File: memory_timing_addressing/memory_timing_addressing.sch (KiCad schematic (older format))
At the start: 1 part, among them P1 DIN_41612_128P

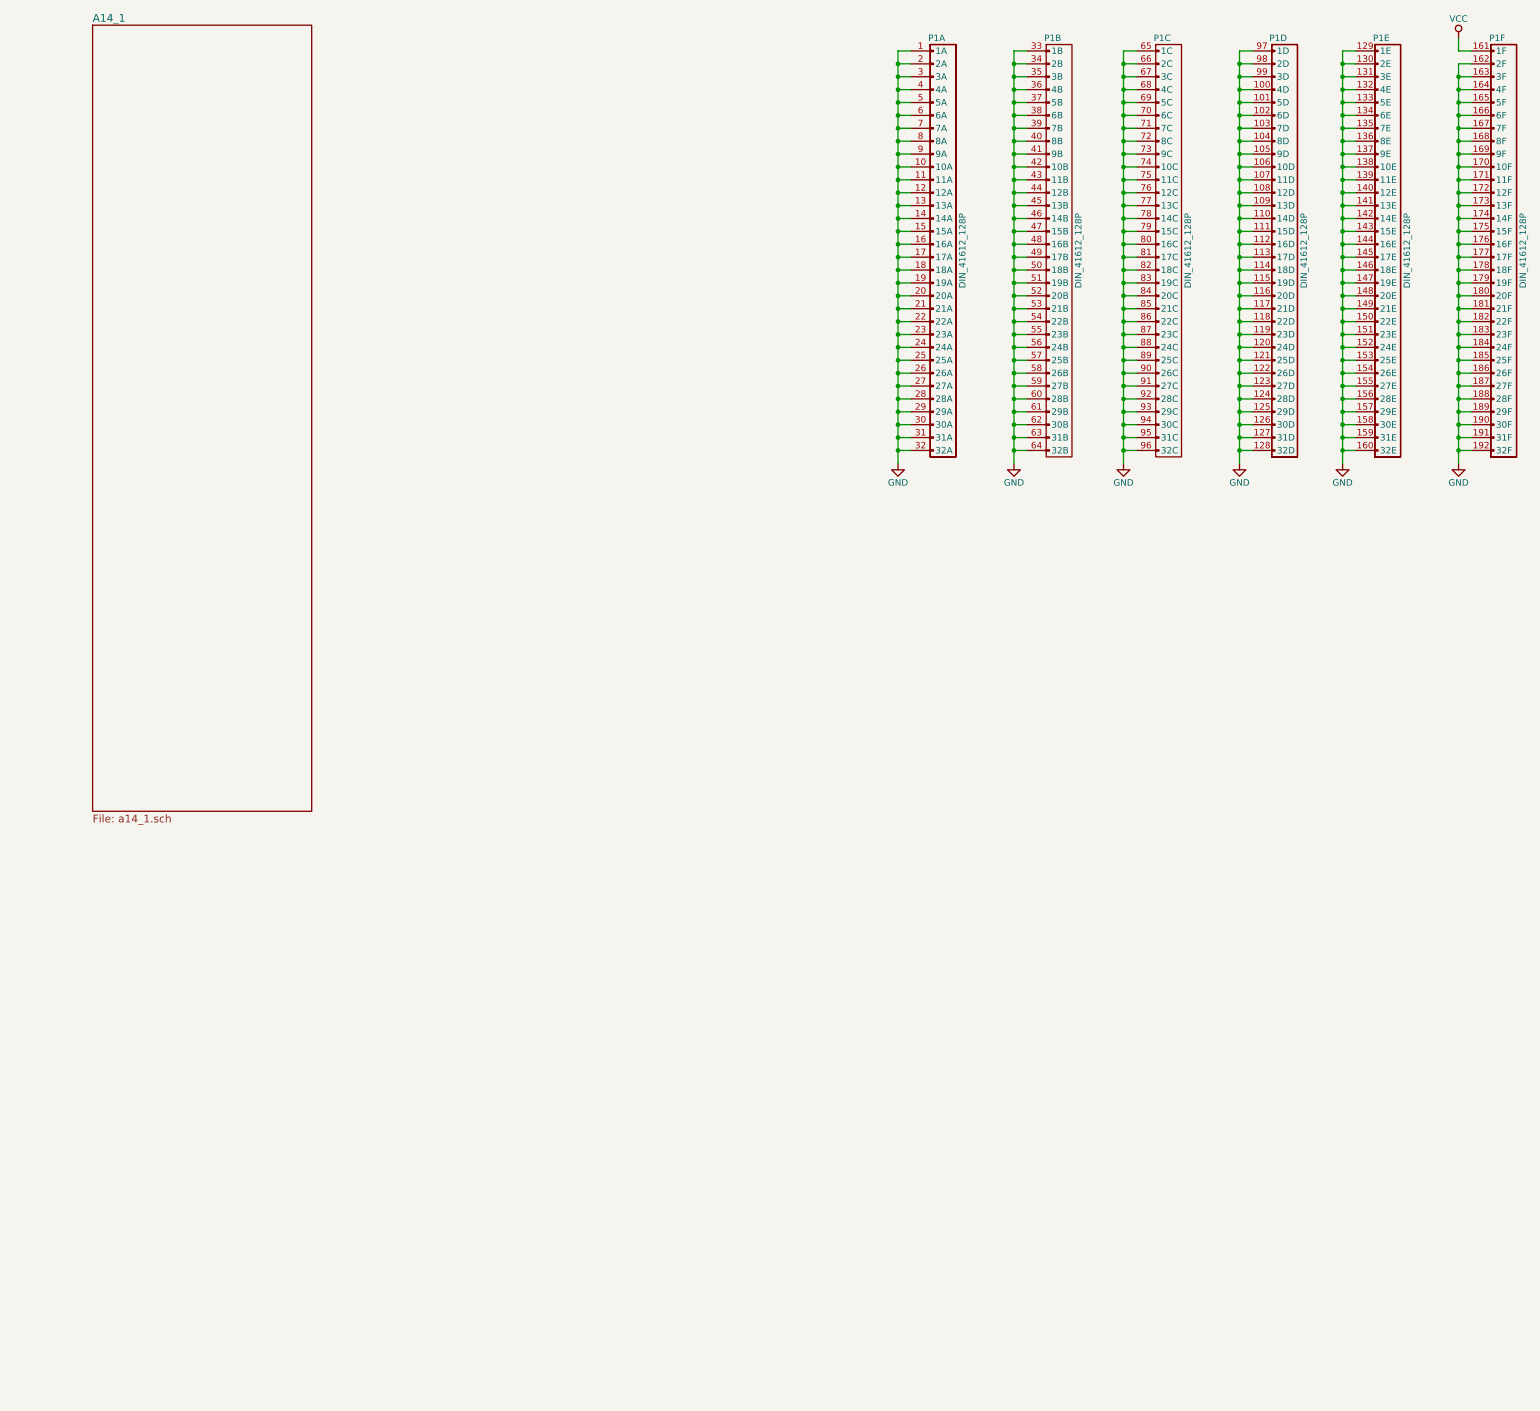
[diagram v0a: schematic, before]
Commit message: Finished off and integrated module 14. Also fixed a couple of bugs this turned up (both initial conditions, and bad wiring in the CGMC pulse generator and S register)
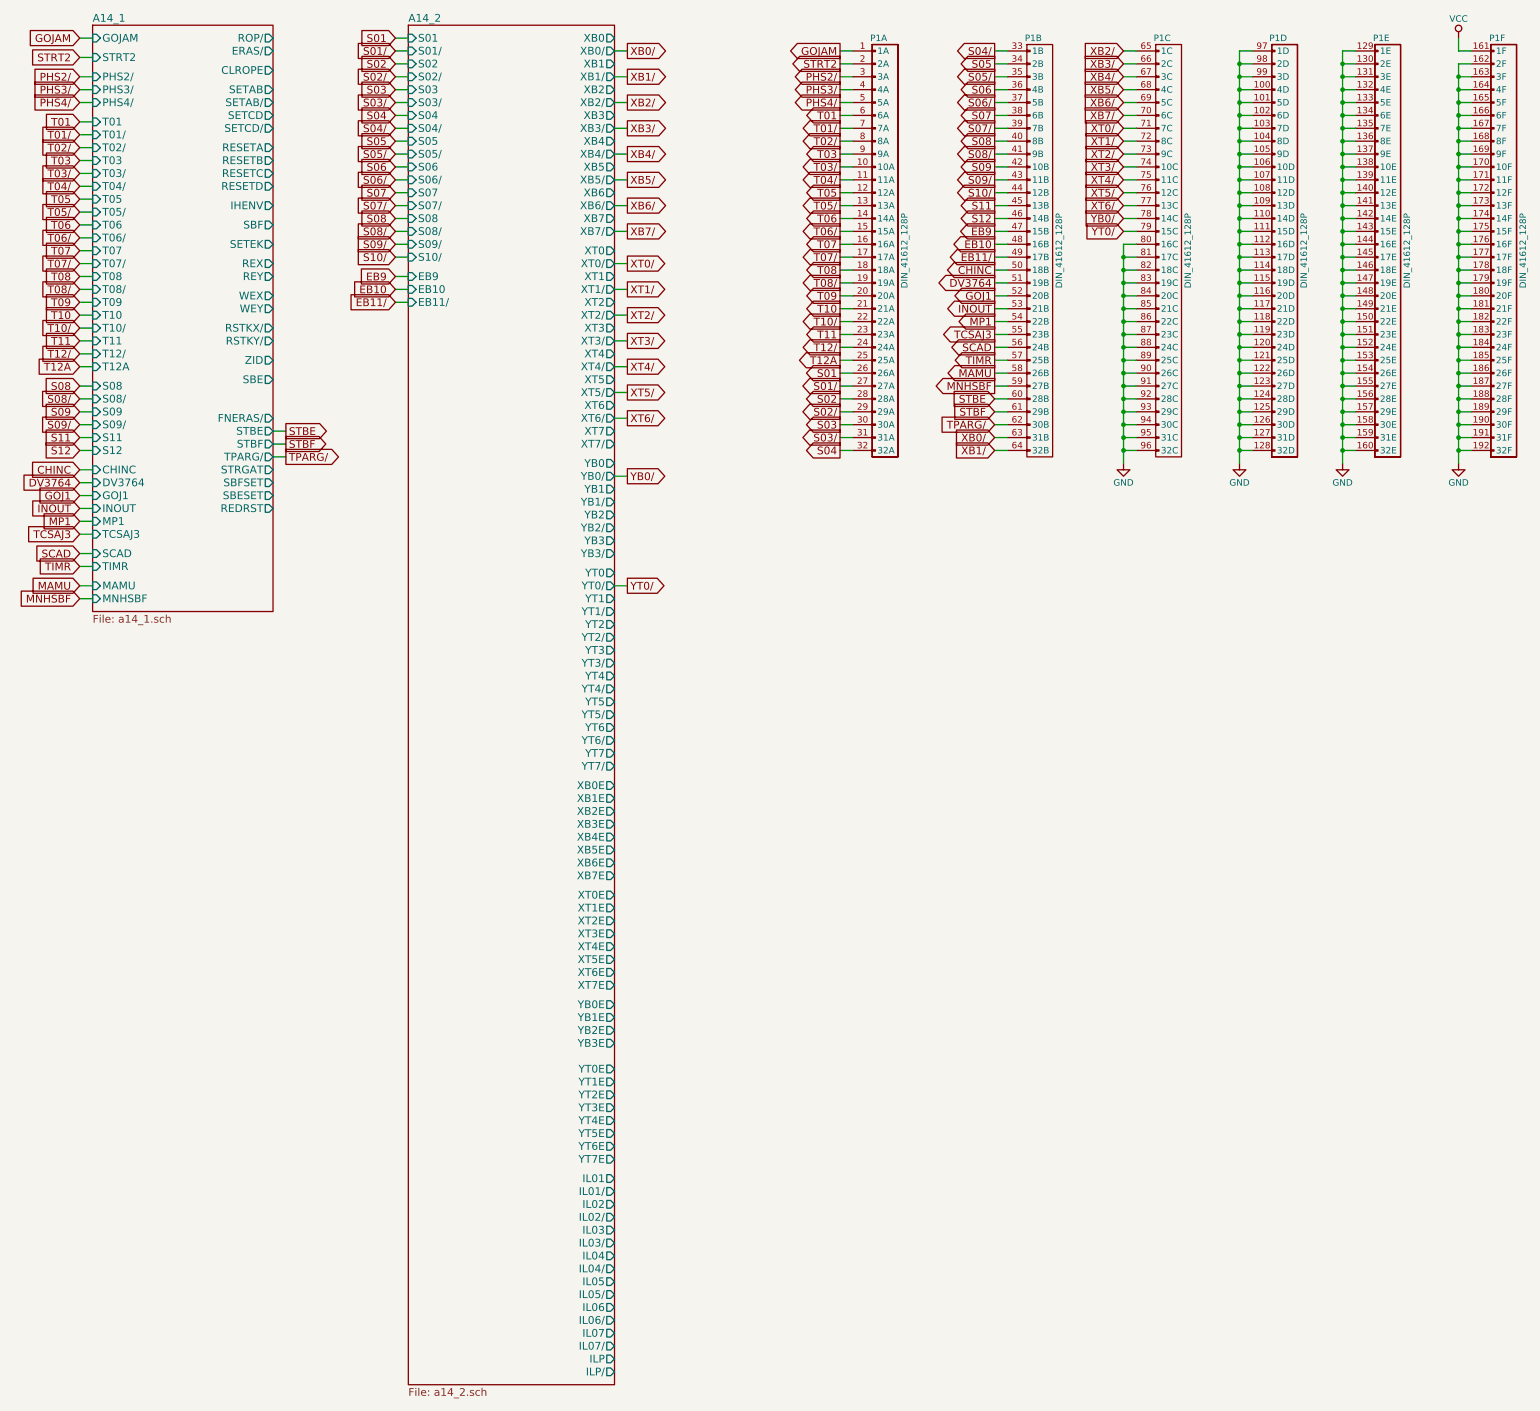
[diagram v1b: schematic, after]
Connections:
- net GND: no longer P1.1 (1A), P1.10 (10A), P1.11 (11A), P1.12 (12A), P1.13 (13A), P1.14 (14A), P1.15 (15A), P1.16 (16A), P1.17 (17A), P1.18 (18A), P1.19 (19A), P1.2 (2A), P1.20 (20A), P1.21 (21A), P1.22 (22A), P1.23 (23A), P1.24 (24A), P1.25 (25A), P1.26 (26A), P1.27 (27A), P1.28 (28A), P1.29 (29A), P1.3 (3A), P1.30 (30A), P1.31 (31A), P1.32 (32A), P1.33 (1B), P1.34 (2B), P1.35 (3B), P1.36 (4B), P1.37 (5B), P1.38 (6B), P1.39 (7B), P1.4 (4A), P1.40 (8B), P1.41 (9B), P1.42 (10B), P1.43 (11B), P1.44 (12B), P1.45 (13B), P1.46 (14B), P1.47 (15B), P1.48 (16B), P1.49 (17B), P1.5 (5A), P1.50 (18B), P1.51 (19B), P1.52 (20B), P1.53 (21B), P1.54 (22B), P1.55 (23B), P1.56 (24B), P1.57 (25B), P1.58 (26B), P1.59 (27B), P1.6 (6A), P1.60 (28B), P1.61 (29B), P1.62 (30B), P1.63 (31B), P1.64 (32B), P1.65 (1C), P1.66 (2C), P1.67 (3C), P1.68 (4C), P1.69 (5C), P1.7 (7A), P1.70 (6C), P1.71 (7C), P1.72 (8C), P1.73 (9C), P1.74 (10C), P1.75 (11C), P1.76 (12C), P1.77 (13C), P1.78 (14C), P1.79 (15C), P1.8 (8A), P1.9 (9A)
- new net CHINC: P1.50 (18B)
- new net DV3764: P1.51 (19B)
- new net EB10: P1.48 (16B)
- new net EB11/: P1.49 (17B)
- new net EB9: P1.47 (15B)
- new net GOJ1: P1.52 (20B)
- new net GOJAM: P1.1 (1A)
- new net INOUT: P1.53 (21B)
- new net MAMU: P1.58 (26B)
- new net MNHSBF: P1.59 (27B)
- new net MP1: P1.54 (22B)
- new net PHS2/: P1.3 (3A)
- new net PHS3/: P1.4 (4A)
- new net PHS4/: P1.5 (5A)
- new net S01: P1.26 (26A)
- new net S01/: P1.27 (27A)
- new net S02: P1.28 (28A)
- new net S02/: P1.29 (29A)
- new net S03: P1.30 (30A)
- new net S03/: P1.31 (31A)
- new net S04: P1.32 (32A)
- new net S04/: P1.33 (1B)
- new net S05: P1.34 (2B)
- new net S05/: P1.35 (3B)
- new net S06: P1.36 (4B)
- new net S06/: P1.37 (5B)
- new net S07: P1.38 (6B)
- new net S07/: P1.39 (7B)
- new net S08: P1.40 (8B)
- new net S08/: P1.41 (9B)
- new net S09: P1.42 (10B)
- new net S09/: P1.43 (11B)
- new net S10/: P1.44 (12B)
- new net S11: P1.45 (13B)
- new net S12: P1.46 (14B)
- new net SCAD: P1.56 (24B)
- new net STBE: P1.60 (28B)
- new net STBF: P1.61 (29B)
- new net STRT2: P1.2 (2A)
- new net T01: P1.6 (6A)
- new net T01/: P1.7 (7A)
- new net T02/: P1.8 (8A)
- new net T03: P1.9 (9A)
- new net T03/: P1.10 (10A)
- new net T04/: P1.11 (11A)
- new net T05: P1.12 (12A)
- new net T05/: P1.13 (13A)
- new net T06: P1.14 (14A)
- new net T06/: P1.15 (15A)
- new net T07: P1.16 (16A)
- new net T07/: P1.17 (17A)
- new net T08: P1.18 (18A)
- new net T08/: P1.19 (19A)
- new net T09: P1.20 (20A)
- new net T10: P1.21 (21A)
- new net T10/: P1.22 (22A)
- new net T11: P1.23 (23A)
- new net T12/: P1.24 (24A)
- new net T12A: P1.25 (25A)
- new net TCSAJ3: P1.55 (23B)
- new net TIMR: P1.57 (25B)
- new net TPARG/: P1.62 (30B)
- new net XB0/: P1.63 (31B)
- new net XB1/: P1.64 (32B)
- new net XB2/: P1.65 (1C)
- new net XB3/: P1.66 (2C)
- new net XB4/: P1.67 (3C)
- new net XB5/: P1.68 (4C)
- new net XB6/: P1.69 (5C)
- new net XB7/: P1.70 (6C)
- new net XT0/: P1.71 (7C)
- new net XT1/: P1.72 (8C)
- new net XT2/: P1.73 (9C)
- new net XT3/: P1.74 (10C)
- new net XT4/: P1.75 (11C)
- new net XT5/: P1.76 (12C)
- new net XT6/: P1.77 (13C)
- new net YB0/: P1.78 (14C)
- new net YT0/: P1.79 (15C)
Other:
- moved on the sheet: P1A, P1B

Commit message: Added and tied in module 15, the rupt service (and banking/rope+strand selection)
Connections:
- net GND: no longer P1.80 (16C)
- net TPARG/: now also P1.63 (31B); no longer P1.62 (30B)
- net XB0/: now also P1.64 (32B); no longer P1.63 (31B)
- net XB1/: now also P1.65 (1C); no longer P1.64 (32B)
- net XB2/: now also P1.66 (2C); no longer P1.65 (1C)
- net XB3/: now also P1.67 (3C); no longer P1.66 (2C)
- net XB4/: now also P1.68 (4C); no longer P1.67 (3C)
- net XB5/: now also P1.69 (5C); no longer P1.68 (4C)
- net XB6/: now also P1.70 (6C); no longer P1.69 (5C)
- net XB7/: now also P1.71 (7C); no longer P1.70 (6C)
- net XT0/: now also P1.72 (8C); no longer P1.71 (7C)
- net XT1/: now also P1.73 (9C); no longer P1.72 (8C)
- net XT2/: now also P1.74 (10C); no longer P1.73 (9C)
- net XT3/: now also P1.75 (11C); no longer P1.74 (10C)
- net XT4/: now also P1.76 (12C); no longer P1.75 (11C)
- net XT5/: now also P1.77 (13C); no longer P1.76 (12C)
- net XT6/: now also P1.78 (14C); no longer P1.77 (13C)
- net YB0/: now also P1.79 (15C); no longer P1.78 (14C)
- net YT0/: now also P1.80 (16C); no longer P1.79 (15C)
- new net STRGAT: P1.62 (30B)
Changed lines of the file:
@@
 Wire Wire Line
 	9450 3000 9550 3000
-Connection ~ 9450 3000
 Wire Wire Line
 	9450 3100 9550 3100
@@
 STBF
 Wire Wire Line
-	8550 4300 8450 4300
-Text GLabel 8450 4300 0    60   Input ~ 0
+	8550 4400 8450 4400
+Text GLabel 8450 4400 0    60   Input ~ 0
 TPARG/
 Wire Wire Line
@@
 XB7/
 Wire Wire Line
-	8550 4400 8450 4400
-Text GLabel 8450 4400 0    60   Input ~ 0
-XB0/
-Wire Wire Line
 	8550 4500 8450 4500
 Text GLabel 8450 4500 0    60   Input ~ 0
-XB1/
+XB0/
 Wire Wire Line
 	9550 1400 9450 1400
 Text GLabel 9450 1400 0    60   Input ~ 0
-XB2/
+XB1/
 Wire Wire Line
 	9550 1500 9450 1500
 Text GLabel 9450 1500 0    60   Input ~ 0
-XB3/
+XB2/
 Wire Wire Line
 	9550 1600 9450 1600
 Text GLabel 9450 1600 0    60   Input ~ 0
-XB4/
+XB3/
 Wire Wire Line
 	9550 1700 9450 1700
 Text GLabel 9450 1700 0    60   Input ~ 0
-XB5/
+XB4/
 Wire Wire Line
 	9550 1800 9450 1800
 Text GLabel 9450 1800 0    60   Input ~ 0
-XB6/
+XB5/
 Wire Wire Line
 	9550 1900 9450 1900
 Text GLabel 9450 1900 0    60   Input ~ 0
+XB6/
+Wire Wire Line
+	9550 2000 9450 2000
+Text GLabel 9450 2000 0    60   Input ~ 0
 XB7/
 Wire Wire Line
@@
 XT6/
 Wire Wire Line
-	9550 2000 9450 2000
-Text GLabel 9450 2000 0    60   Input ~ 0
-XT0/
-Wire Wire Line
 	9550 2100 9450 2100
 Text GLabel 9450 2100 0    60   Input ~ 0
-XT1/
+XT0/
 Wire Wire Line
 	9550 2200 9450 2200
 Text GLabel 9450 2200 0    60   Input ~ 0
-XT2/
+XT1/
 Wire Wire Line
 	9550 2300 9450 2300
 Text GLabel 9450 2300 0    60   Input ~ 0
-XT3/
+XT2/
 Wire Wire Line
 	9550 2400 9450 2400
 Text GLabel 9450 2400 0    60   Input ~ 0
-XT4/
+XT3/
 Wire Wire Line
 	9550 2500 9450 2500
 Text GLabel 9450 2500 0    60   Input ~ 0
-XT5/
+XT4/
 Wire Wire Line
 	9550 2600 9450 2600
 Text GLabel 9450 2600 0    60   Input ~ 0
+XT5/
+Wire Wire Line
+	9550 2700 9450 2700
+Text GLabel 9450 2700 0    60   Input ~ 0
 XT6/
 Wire Wire Line
@@
 YB0/
 Wire Wire Line
-	9550 2700 9450 2700
-Text GLabel 9450 2700 0    60   Input ~ 0
+	9550 2800 9450 2800
+Text GLabel 9450 2800 0    60   Input ~ 0
 YB0/
 Wire Wire Line
@@
 YT0/
 Wire Wire Line
-	9550 2800 9450 2800
-Text GLabel 9450 2800 0    60   Input ~ 0
+	9550 2900 9450 2900
+Text GLabel 9450 2900 0    60   Input ~ 0
 YT0/
 Wire Wire Line
-	9550 2900 9450 2900
-Wire Wire Line
-	9450 2900 9450 4600
+	2850 4650 2950 4650
+Text GLabel 2950 4650 2    60   Output ~ 0
+STRGAT
+Wire Wire Line
+	9450 3000 9450 4600
+Wire Wire Line
+	8550 4300 8450 4300
+Text GLabel 8450 4300 0    60   Input ~ 0
+STRGAT
 $EndSCHEMATC
